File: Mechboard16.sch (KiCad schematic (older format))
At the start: 154 parts, among them CN1 CONN_C16, CN2 CONN_+4, SW0:0 KEY_DEL, SW0:1 KEY_RET, SW0:2 KEY_PND, SW0:3 KEY_HLP, SW0:4 KEY_F1, SW0:5 KEY_F2, SW0:6 KEY_F3, SW0:7 KEY_AT, SW1:0 KEY_3, SW1:1 KEY_W, SW1:2 KEY_A, SW1:3 KEY_4, SW1:4 KEY_Z, SW1:5 KEY_S, SW1:6 KEY_E, SW1:7 KEY_LSH, SW1B:7 KEY_RSH, SW1C:7 KEY_CLK, SW2:0 KEY_5, SW2:1 KEY_R, SW2:2 KEY_D, SW2:3 KEY_6, SW2:4 KEY_C, SW2:5 KEY_F, SW2:6 KEY_T, SW2:7 KEY_X, SW3:0 KEY_7, SW3:1 KEY_Y, SW3:2 KEY_G, SW3:3 KEY_8, SW3:4 KEY_B, SW3:5 KEY_H, SW3:6 KEY_U, SW3:7 KEY_V, SW4:0 KEY_9, SW4:1 KEY_I, SW4:2 KEY_J, SW4:3 KEY_0, SW4:4 KEY_M, SW4:5 KEY_K, SW4:6 KEY_O, SW4:7 KEY_N, SW5:0 KEY_DN, SW5:1 KEY_P, SW5:2 KEY_L, SW5:3 KEY_UP, SW5:4 KEY_DOT, SW5:5 KEY_COL, SW5:6 KEY_MIN, SW5:7 KEY_COM, SW6:0 KEY_LF, SW6:1 KEY_AST, SW6:2 KEY_SEM, SW6:3 KEY_RT, SW6:4 KEY_ESC, SW6:5 KEY_EQ, SW6:6 KEY_PLS, SW6:7 KEY_SLA, SW7:0 KEY_1, SW7:1 KEY_CLR, SW7:2 KEY_CTL, SW7:3 KEY_2, SW7:4 KEY_SPC, SW7:5 KEY_CMD, SW7:6 KEY_Q, SW7:7 KEY_RUN, SW7B:2 KEY_CTL_2, U1 4066, U2 NE555, U3 RP2040_Zero

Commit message: Add ATmega32U4, MAX7221 and leeeeeds! Routing TBD ^___^
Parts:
- removed SW7B:2: KEY_CTL_2, Mechboard16:SW_Cherry_MX_PCB_1.50u, symbol Switch:SW_Push_45deg
- removed U3: RP2040_Zero, Mechboard16:rp2040-zero, symbol RP2040_Zero:RP2040_Zero
- LD1: value LED -> LED_CLK
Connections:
- net labels added: col[0..7], row[0..7]
- wire segments 469 -> 462
- no-connect marks 14 -> 9
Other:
- note removed: "NOTE: If U3 is mounted, do NOT \nconnect keyboard to computer\nvia CN1/2!"
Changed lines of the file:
@@
 $Descr A4 11693 8268
 encoding utf-8
-Sheet 1 1
+Sheet 1 2
 Title "Mechboard16"
-Date "2023-10-13"
+Date "2023-11-25"
 Rev "1git"
 Comp "SukkoPera"
@@
 	5260 6850 5680 6850
 $Comp
-L power:GND #PWR0103
+L power:GND #PWR06
 U 1 1 66EB0AEA
 P 5260 7470
-F 0 "#PWR0103" H 5260 7220 50  0001 C CNN
+F 0 "#PWR06" H 5260 7220 50  0001 C CNN
 F 1 "GND" H 5265 7297 50  0000 C CNN
 F 2 "" H 5260 7470 50  0001 C CNN
@@
 	6465 2880 6770 2880
 $Comp
-L power:GND #PWR0104
+L power:GND #PWR05
 U 1 1 67015259
 P 6465 4160
-F 0 "#PWR0104" H 6465 3910 50  0001 C CNN
+F 0 "#PWR05" H 6465 3910 50  0001 C CNN
 F 1 "GND" H 6470 3987 50  0000 C CNN
 F 2 "" H 6465 4160 50  0001 C CNN
@@
 	1    0    0    -1
 $EndComp
-Wire Wire Line
-	7245 3600 7245 3650
 $Comp
 L power:GND #PWR0107
@@
 P 9670 5870
 F 0 "LD1" V 9709 5752 50  0000 R CNN
-F 1 "LED" V 9618 5752 50  0000 R CNN
+F 1 "LED_CLK" V 9618 5752 50  0000 R CNN
 F 2 "LED_THT:LED_D3.0mm" H 9670 5870 50  0001 C CNN
 F 3 "~" H 9670 5870 50  0001 C CNN
@@
 Wire Wire Line
 	7245 3235 7245 3175
-$Comp
-L power:PWR_FLAG #FLG0102
-U 1 1 680610F8
-P 7245 3650
-F 0 "#FLG0102" H 7245 3725 50  0001 C CNN
-F 1 "PWR_FLAG" V 7245 3778 50  0000 L CNN
-F 2 "" H 7245 3650 50  0001 C CNN
-F 3 "~" H 7245 3650 50  0001 C CNN
-	1    7245 3650
-	0    1    1    0
-$EndComp
-Connection ~ 7245 3650
-Wire Wire Line
-	7245 3650 7245 3695
 Text Notes 8205 1225 2    50   ~ 0
 Note that the C16 does not\nhave power on the keyboard\nconnector! A bodge wire mod\nwill be needed!\nFor LittleSixteen, we'll add a\njumper in the next release.
@@
 	0    1    1    0
 $EndComp
+Text Notes 3825 6255 0    50   ~ 0
+MOUNTING\nHOLES
+Text Label 2675 4835 0    50   ~ 0
+ctl_a
+Text Label 2875 5235 1    50   ~ 0
+ctl_b
+$Sheet
+S 1460 7125 955  490
+U 656CF65E
+F0 "USB Controller" 50
+F1 "usb.sch" 50
+$EndSheet
+Text GLabel 2655 5975 2    50   Output ~ 0
+col[0..7]
+Wire Bus Line
+	2190 5975 2655 5975
+Entry Wire Line
+	2190 6805 2290 6905
+Entry Wire Line
+	2190 6705 2290 6805
+Entry Wire Line
+	2190 6605 2290 6705
+Entry Wire Line
+	2190 6505 2290 6605
+Entry Wire Line
+	2190 6405 2290 6505
+Entry Wire Line
+	2190 6305 2290 6405
+Entry Wire Line
+	2190 6205 2290 6305
+Entry Wire Line
+	2190 6105 2290 6205
+Text GLabel 1250 5975 0    50   BiDi ~ 0
+row[0..7]
+Wire Bus Line
+	1715 5975 1250 5975
+Entry Wire Line
+	1715 6805 1615 6905
+Entry Wire Line
+	1715 6705 1615 6805
+Entry Wire Line
+	1715 6605 1615 6705
+Entry Wire Line
+	1715 6505 1615 6605
+Entry Wire Line
+	1715 6405 1615 6505
+Entry Wire Line
+	1715 6305 1615 6405
+Entry Wire Line
+	1715 6205 1615 6305
+Entry Wire Line
+	1715 6105 1615 6205
+Text Notes 1440 5610 0    50   ~ 0
+USB KEYBOARD CONTROLLER
+Text Label 2675 6205 2    50   ~ 0
+col7
+Text Label 2675 6305 2    50   ~ 0
+col6
+Text Label 2675 6405 2    50   ~ 0
+col5
+Text Label 2675 6505 2    50   ~ 0
+col4
+Text Label 2675 6605 2    50   ~ 0
+col3
+Text Label 2675 6705 2    50   ~ 0
+col2
+Text Label 2675 6805 2    50   ~ 0
+col1
+Text Label 2675 6905 2    50   ~ 0
+col0
+Text Label 1230 6905 0    50   ~ 0
+row7
+Text Label 1230 6805 0    50   ~ 0
+row6
+Text Label 1230 6705 0    50   ~ 0
+row5
+Text Label 1230 6605 0    50   ~ 0
+row4
+Text Label 1230 6505 0    50   ~ 0
+row3
+Text Label 1230 6405 0    50   ~ 0
+row2
+Text Label 1230 6305 0    50   ~ 0
+row1
+Text Label 1230 6205 0    50   ~ 0
+row0
 Wire Wire Line
-	950  6055 850  6055
-Wire Wire Line
-	850  6055 850  5755
-Wire Wire Line
-	950  6155 850  6155
-Wire Wire Line
-	850  6155 850  7405
-$Comp
-L power:GND #PWR06
-U 1 1 68E3A75D
-P 850 7405
-F 0 "#PWR06" H 850 7155 50  0001 C CNN
-F 1 "GND" H 855 7232 50  0000 C CNN
-F 2 "" H 850 7405 50  0001 C CNN
-F 3 "" H 850 7405 50  0001 C CNN
-	1    850  7405
-	1    0    0    -1
-$EndComp
-$Comp
-L power:+5V #PWR05
-U 1 1 68E3AF82
-P 850 5755
-F 0 "#PWR05" H 850 5605 50  0001 C CNN
-F 1 "+5V" H 865 5928 50  0000 C CNN
-F 2 "" H 850 5755 50  0001 C CNN
-F 3 "" H 850 5755 50  0001 C CNN
-	1    850  5755
-	1    0    0    -1
-$EndComp
-NoConn ~ 950  6255
-NoConn ~ 950  6355
-NoConn ~ 950  6455
-NoConn ~ 950  6555
-NoConn ~ 950  6655
-Wire Wire Line
-	2950 6055 3335 6055
-Wire Wire Line
-	2950 6155 3335 6155
+	2675 6805 2290 6805
 Wire Wire Line
-	2950 6255 3335 6255
+	2675 6705 2290 6705
 Wire Wire Line
-	2950 6355 3335 6355
+	2675 6605 2290 6605
 Wire Wire Line
-	2950 6455 3335 6455
+	2675 6505 2290 6505
 Wire Wire Line
-	2950 6555 3335 6555
+	2675 6405 2290 6405
 Wire Wire Line
-	2950 6655 3335 6655
+	2675 6305 2290 6305
 Wire Wire Line
-	2950 6755 3335 6755
+	2675 6205 2290 6205
 Wire Wire Line
-	2950 6855 3335 6855
+	2290 6905 2675 6905
 Wire Wire Line
-	565  6755 950  6755
+	1615 6905 1230 6905
 Wire Wire Line
-	565  6855 950  6855
+	1615 6805 1230 6805
 Wire Wire Line
-	1750 7740 1750 7355
+	1615 6705 1230 6705
 Wire Wire Line
-	1850 7740 1850 7355
+	1615 6605 1230 6605
 Wire Wire Line
-	1950 7740 1950 7355
+	1615 6505 1230 6505
 Wire Wire Line
-	2050 7740 2050 7355
+	1615 6405 1230 6405
 Wire Wire Line
-	2150 7740 2150 7355
-Text Label 3335 6055 2    50   ~ 0
-row0
-Text Label 3335 6155 2    50   ~ 0
-row1
-Text Label 3335 6255 2    50   ~ 0
-row2
-Text Label 3335 6355 2    50   ~ 0
-row3
-Text Label 3335 6455 2    50   ~ 0
-row4
-Text Label 3335 6555 2    50   ~ 0
-row5
-Text Label 3335 6655 2    50   ~ 0
-row6
-Text Label 3335 6755 2    50   ~ 0
-row7
-Text Label 3335 6855 2    50   ~ 0
-col0
-Text Label 2150 7740 1    50   ~ 0
-col1
-Text Label 2050 7740 1    50   ~ 0
-col2
-Text Label 1950 7740 1    50   ~ 0
-col3
-Text Label 1850 7740 1    50   ~ 0
-col4
-Text Label 1750 7740 1    50   ~ 0
-col5
-Text Label 565  6855 0    50   ~ 0
-col6
-Text Label 565  6755 0    50   ~ 0
-col7
-Text Notes 3825 6255 0    50   ~ 0
-MOUNTING\nHOLES
-Text Notes 1440 5610 0    50   ~ 0
-USB KEYBOARD CONTROLLER
-Text Notes 2275 7395 0    50   ~ 0
-NOTE: If U3 is mounted, do NOT \nconnect keyboard to computer\nvia CN1/2!
-$Comp
-L RP2040_Zero:RP2040_Zero U3
-U 1 1 68DDCE04
-P 1950 6455
-F 0 "U3" H 1950 7220 50  0000 C CNN
-F 1 "RP2040_Zero" H 1950 7129 50  0000 C CNN
-F 2 "Mechboard16:rp2040-zero" H 1950 6455 50  0001 C CNN
-F 3 "https://www.waveshare.com/wiki/RP2040-Zero" H 1950 6455 50  0001 C CNN
-	1    1950 6455
-	1    0    0    -1
-$EndComp
-$Comp
-L Switch:SW_Push_45deg SW7B:2
-U 1 1 6971412A
-P 6200 980
-F 0 "SW7B:2" H 6275 1135 50  0000 C CIN
-F 1 "KEY_CTL_2" V 6020 980 50  0000 C CNN
-F 2 "Mechboard16:SW_Cherry_MX_PCB_1.50u" H 6200 980 50  0001 C CNN
-F 3 "~" H 6200 980 50  0001 C CNN
-	1    6200 980
-	1    0    0    -1
-$EndComp
+	1615 6305 1230 6305
 Wire Wire Line
-	6100 880  6100 775
-Text Label 6100 775  0    50   ~ 0
-ctl_a
-Text Label 2675 4835 0    50   ~ 0
-ctl_a
-Text Label 2875 5235 1    50   ~ 0
-ctl_b
-Text Label 6515 1080 2    50   ~ 0
-ctl_b
+	1615 6205 1230 6205
 Wire Wire Line
-	6300 1080 6515 1080
+	7245 3600 7245 3695
+Wire Bus Line
+	2190 5975 2190 6805
+Wire Bus Line
+	1715 5975 1715 6805
 $EndSCHEMATC

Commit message: LED routing in progress...
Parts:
- SW0:3, SW0:4, SW0:5, SW0:6, SW1:7, SW1B:7, SW7:2: footprint Mechboard16:SW_Cherry_MX_PCB_1.50u -> Mechboard16:SW_Cherry_MX_PCB_1.50u_OffsetR
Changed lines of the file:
@@
 F 0 "SW7:2" H 2855 5190 50  0000 C CNN
 F 1 "KEY_CTL" V 2595 5035 50  0000 C CNN
-F 2 "Mechboard16:SW_Cherry_MX_PCB_1.50u" H 2775 5035 50  0001 C CNN
+F 2 "Mechboard16:SW_Cherry_MX_PCB_1.50u_OffsetR" H 2775 5035 50  0001 C CNN
 F 3 "~" H 2775 5035 50  0001 C CNN
 	1    2775 5035
@@
 F 0 "SW0:3" H 3350 1690 50  0000 C CNN
 F 1 "KEY_HLP" V 3095 1535 50  0000 C CNN
-F 2 "Mechboard16:SW_Cherry_MX_PCB_1.50u" H 3275 1535 50  0001 C CNN
+F 2 "Mechboard16:SW_Cherry_MX_PCB_1.50u_OffsetR" H 3275 1535 50  0001 C CNN
 F 3 "~" H 3275 1535 50  0001 C CNN
 	1    3275 1535
@@
 F 0 "SW0:4" H 3850 1690 50  0000 C CNN
 F 1 "KEY_F1" V 3595 1535 50  0000 C CNN
-F 2 "Mechboard16:SW_Cherry_MX_PCB_1.50u" H 3775 1535 50  0001 C CNN
+F 2 "Mechboard16:SW_Cherry_MX_PCB_1.50u_OffsetR" H 3775 1535 50  0001 C CNN
 F 3 "~" H 3775 1535 50  0001 C CNN
 	1    3775 1535
@@
 F 0 "SW0:5" H 4350 1690 50  0000 C CNN
 F 1 "KEY_F2" V 4095 1535 50  0000 C CNN
-F 2 "Mechboard16:SW_Cherry_MX_PCB_1.50u" H 4275 1535 50  0001 C CNN
+F 2 "Mechboard16:SW_Cherry_MX_PCB_1.50u_OffsetR" H 4275 1535 50  0001 C CNN
 F 3 "~" H 4275 1535 50  0001 C CNN
 	1    4275 1535
@@
 F 0 "SW0:6" H 4850 1690 50  0000 C CNN
 F 1 "KEY_F3" V 4595 1535 50  0000 C CNN
-F 2 "Mechboard16:SW_Cherry_MX_PCB_1.50u" H 4775 1535 50  0001 C CNN
+F 2 "Mechboard16:SW_Cherry_MX_PCB_1.50u_OffsetR" H 4775 1535 50  0001 C CNN
 F 3 "~" H 4775 1535 50  0001 C CNN
 	1    4775 1535
@@
 F 0 "SW1:7" H 5355 2190 50  0000 C CNN
 F 1 "KEY_LSH" V 5095 2035 50  0000 C CNN
-F 2 "Mechboard16:SW_Cherry_MX_PCB_1.50u" H 5275 2035 50  0001 C CNN
+F 2 "Mechboard16:SW_Cherry_MX_PCB_1.50u_OffsetR" H 5275 2035 50  0001 C CNN
 F 3 "~" H 5275 2035 50  0001 C CNN
 	1    5275 2035
@@
 F 0 "SW1B:7" H 5855 2190 50  0000 C CNN
 F 1 "KEY_RSH" V 5595 2035 50  0000 C CNN
-F 2 "Mechboard16:SW_Cherry_MX_PCB_1.50u" H 5775 2035 50  0001 C CNN
+F 2 "Mechboard16:SW_Cherry_MX_PCB_1.50u_OffsetR" H 5775 2035 50  0001 C CNN
 F 3 "~" H 5775 2035 50  0001 C CNN
 	1    5775 2035

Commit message: Routing in progress
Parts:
- SW7:4: footprint Mechboard16:SW_Cherry_MX_PCB_1.00u -> Mechboard16:SW_Cherry_MX_PCB_9.00u
- renumbered LD1 to LD1C:7
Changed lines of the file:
@@
 F 0 "SW7:4" H 3855 5190 50  0000 C CNN
 F 1 "KEY_SPC" V 3595 5035 50  0000 C CNN
-F 2 "Mechboard16:SW_Cherry_MX_PCB_1.00u" H 3775 5035 50  0001 C CNN
+F 2 "Mechboard16:SW_Cherry_MX_PCB_9.00u" H 3775 5035 50  0001 C CNN
 F 3 "~" H 3775 5035 50  0001 C CNN
 	1    3775 5035
@@
 	9670 5665 9670 5720
 $Comp
-L Device:LED LD1
+L Device:LED LD1C:7
 U 1 1 6726E132
 P 9670 5870
-F 0 "LD1" V 9709 5752 50  0000 R CNN
+F 0 "LD1C:7" V 9709 5752 50  0000 R CNN
 F 1 "LED_CLK" V 9618 5752 50  0000 R CNN
 F 2 "LED_THT:LED_D3.0mm" H 9670 5870 50  0001 C CNN

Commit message: IN PRODUCTION!
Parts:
- R3: value 56 -> 1k; LCSC C17557 -> C17513
- U1: LCSC C412482 -> C233577
- U2: LCSC C181735 -> C5125085
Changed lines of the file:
@@
 F 2 "Package_SO:SOIC-14_3.9x8.7mm_P1.27mm" H 10225 5235 50  0001 C CNN
 F 3 "http://www.ti.com/lit/ds/symlink/cd4066b.pdf" H 10225 5235 50  0001 C CNN
-F 4 "C412482" H 10225 5235 50  0001 C CNN "LCSC"
+F 4 "C233577" H 10225 5235 50  0001 C CNN "LCSC"
 	1    10225 5235
 	0    -1   -1   0
@@
 F 2 "Package_SO:SOIC-14_3.9x8.7mm_P1.27mm" H 5680 7260 50  0001 C CNN
 F 3 "http://www.ti.com/lit/ds/symlink/cd4066b.pdf" H 5680 7260 50  0001 C CNN
-F 4 "C412482" H 5680 7260 50  0001 C CNN "LCSC"
+F 4 "C233577" H 5680 7260 50  0001 C CNN "LCSC"
 	2    5680 7260
 	1    0    0    -1
@@
 F 2 "Package_SO:SOIC-14_3.9x8.7mm_P1.27mm" H 4855 7260 50  0001 C CNN
 F 3 "http://www.ti.com/lit/ds/symlink/cd4066b.pdf" H 4855 7260 50  0001 C CNN
-F 4 "C412482" H 4855 7260 50  0001 C CNN "LCSC"
+F 4 "C233577" H 4855 7260 50  0001 C CNN "LCSC"
 	3    4855 7260
 	1    0    0    -1
@@
 F 2 "Package_SO:SOIC-14_3.9x8.7mm_P1.27mm" H 6560 7260 50  0001 C CNN
 F 3 "http://www.ti.com/lit/ds/symlink/cd4066b.pdf" H 6560 7260 50  0001 C CNN
-F 4 "C412482" H 6560 7260 50  0001 C CNN "LCSC"
+F 4 "C233577" H 6560 7260 50  0001 C CNN "LCSC"
 	4    6560 7260
 	1    0    0    -1
@@
 F 2 "Package_SO:SOIC-14_3.9x8.7mm_P1.27mm" H 6155 3440 50  0001 C CNN
 F 3 "http://www.ti.com/lit/ds/symlink/cd4066b.pdf" H 6155 3440 50  0001 C CNN
-F 4 "C412482" H 6155 3440 50  0001 C CNN "LCSC"
+F 4 "C233577" H 6155 3440 50  0001 C CNN "LCSC"
 	5    6155 3440
 	1    0    0    -1
@@
 F 2 "Package_SO:SOIC-8_3.9x4.9mm_P1.27mm" H 9740 5035 50  0001 C CNN
 F 3 "http://www.ti.com/lit/ds/symlink/ne555.pdf" H 9740 5035 50  0001 C CNN
-F 4 "C181735" H 8890 5435 50  0001 C CNN "LCSC"
+F 4 "C5125085" H 8890 5435 50  0001 C CNN "LCSC"
 	1    8890 5435
 	1    0    0    -1
@@
 P 9670 5515
 F 0 "R3" H 9600 5469 50  0000 R CNN
-F 1 "56" H 9600 5560 50  0000 R CNN
+F 1 "1k" H 9600 5560 50  0000 R CNN
 F 2 "Resistor_SMD:R_0805_2012Metric_Pad1.20x1.40mm_HandSolder" V 9600 5515 50  0001 C CNN
 F 3 "~" H 9670 5515 50  0001 C CNN
-F 4 "C17557" H 9670 5515 50  0001 C CNN "LCSC"
+F 4 "C17513" H 9670 5515 50  0001 C CNN "LCSC"
 	1    9670 5515
 	-1   0    0    1

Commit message: R3 done
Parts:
- SW0:0, SW0:2, SW0:7, SW1:0, SW1:1, SW1:2, SW1:3, SW1:4, SW1:5, SW1:6, SW1C:7, SW2:0, SW2:1, SW2:2, SW2:3, SW2:4, SW2:5, SW2:6, SW2:7, SW3:0, SW3:1, SW3:2, SW3:3, SW3:4, SW3:5, SW3:6, SW3:7, SW4:0, SW4:1, SW4:2, SW4:3, SW4:4, SW4:5, SW4:6, SW4:7, SW5:0, SW5:1, SW5:2, SW5:3, SW5:4, SW5:5, SW5:6, SW5:7, SW6:0, SW6:1, SW6:2, SW6:3, SW6:4, SW6:5, SW6:6, SW6:7, SW7:0, SW7:1, SW7:3, SW7:5, SW7:6, SW7:7: footprint Mechboard16:SW_Cherry_MX_PCB_1.00u -> Mechboard16:SW_Hybrid_Cherry_MX_Alps_1.00u

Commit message: Switch non-1.00u keys to hybrid
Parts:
- SW0:1: footprint Mechboard16:SW_Cherry_MX_PCB_2.00u -> Mechboard16:SW_Hybrid_Cherry_MX_Alps_2.00u
- SW0:3, SW0:4, SW0:5, SW0:6, SW1:7, SW1B:7, SW7:2: footprint Mechboard16:SW_Cherry_MX_PCB_1.50u_OffsetR -> Mechboard16:SW_Hybrid_Cherry_MX_Alps_1.50u_OffsetR
- SW7:4: footprint Mechboard16:SW_Cherry_MX_PCB_9.00u -> Mechboard16:SW_Hybrid_Cherry_MX_Alps_9.00u
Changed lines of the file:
@@
 F 0 "SW0:1" H 2350 1690 50  0000 C CNN
 F 1 "KEY_RET" V 2095 1535 50  0000 C CNN
-F 2 "Mechboard16:SW_Cherry_MX_PCB_2.00u" H 2275 1535 50  0001 C CNN
+F 2 "Mechboard16:SW_Hybrid_Cherry_MX_Alps_2.00u" H 2275 1535 50  0001 C CNN
 F 3 "~" H 2275 1535 50  0001 C CNN
 	1    2275 1535
@@
 F 0 "SW7:2" H 2855 5190 50  0000 C CNN
 F 1 "KEY_CTL" V 2595 5035 50  0000 C CNN
-F 2 "Mechboard16:SW_Cherry_MX_PCB_1.50u_OffsetR" H 2775 5035 50  0001 C CNN
+F 2 "Mechboard16:SW_Hybrid_Cherry_MX_Alps_1.50u_OffsetR" H 2775 5035 50  0001 C CNN
 F 3 "~" H 2775 5035 50  0001 C CNN
 	1    2775 5035
@@
 F 0 "SW0:3" H 3350 1690 50  0000 C CNN
 F 1 "KEY_HLP" V 3095 1535 50  0000 C CNN
-F 2 "Mechboard16:SW_Cherry_MX_PCB_1.50u_OffsetR" H 3275 1535 50  0001 C CNN
+F 2 "Mechboard16:SW_Hybrid_Cherry_MX_Alps_1.50u_OffsetR" H 3275 1535 50  0001 C CNN
 F 3 "~" H 3275 1535 50  0001 C CNN
 	1    3275 1535
@@
 F 0 "SW0:4" H 3850 1690 50  0000 C CNN
 F 1 "KEY_F1" V 3595 1535 50  0000 C CNN
-F 2 "Mechboard16:SW_Cherry_MX_PCB_1.50u_OffsetR" H 3775 1535 50  0001 C CNN
+F 2 "Mechboard16:SW_Hybrid_Cherry_MX_Alps_1.50u_OffsetR" H 3775 1535 50  0001 C CNN
 F 3 "~" H 3775 1535 50  0001 C CNN
 	1    3775 1535
@@
 F 0 "SW7:4" H 3855 5190 50  0000 C CNN
 F 1 "KEY_SPC" V 3595 5035 50  0000 C CNN
-F 2 "Mechboard16:SW_Cherry_MX_PCB_9.00u" H 3775 5035 50  0001 C CNN
+F 2 "Mechboard16:SW_Hybrid_Cherry_MX_Alps_9.00u" H 3775 5035 50  0001 C CNN
 F 3 "~" H 3775 5035 50  0001 C CNN
 	1    3775 5035
@@
 F 0 "SW0:5" H 4350 1690 50  0000 C CNN
 F 1 "KEY_F2" V 4095 1535 50  0000 C CNN
-F 2 "Mechboard16:SW_Cherry_MX_PCB_1.50u_OffsetR" H 4275 1535 50  0001 C CNN
+F 2 "Mechboard16:SW_Hybrid_Cherry_MX_Alps_1.50u_OffsetR" H 4275 1535 50  0001 C CNN
 F 3 "~" H 4275 1535 50  0001 C CNN
 	1    4275 1535
@@
 F 0 "SW0:6" H 4850 1690 50  0000 C CNN
 F 1 "KEY_F3" V 4595 1535 50  0000 C CNN
-F 2 "Mechboard16:SW_Cherry_MX_PCB_1.50u_OffsetR" H 4775 1535 50  0001 C CNN
+F 2 "Mechboard16:SW_Hybrid_Cherry_MX_Alps_1.50u_OffsetR" H 4775 1535 50  0001 C CNN
 F 3 "~" H 4775 1535 50  0001 C CNN
 	1    4775 1535
@@
 F 0 "SW1:7" H 5355 2190 50  0000 C CNN
 F 1 "KEY_LSH" V 5095 2035 50  0000 C CNN
-F 2 "Mechboard16:SW_Cherry_MX_PCB_1.50u_OffsetR" H 5275 2035 50  0001 C CNN
+F 2 "Mechboard16:SW_Hybrid_Cherry_MX_Alps_1.50u_OffsetR" H 5275 2035 50  0001 C CNN
 F 3 "~" H 5275 2035 50  0001 C CNN
 	1    5275 2035
@@
 F 0 "SW1B:7" H 5855 2190 50  0000 C CNN
 F 1 "KEY_RSH" V 5595 2035 50  0000 C CNN
-F 2 "Mechboard16:SW_Cherry_MX_PCB_1.50u_OffsetR" H 5775 2035 50  0001 C CNN
+F 2 "Mechboard16:SW_Hybrid_Cherry_MX_Alps_1.50u_OffsetR" H 5775 2035 50  0001 C CNN
 F 3 "~" H 5775 2035 50  0001 C CNN
 	1    5775 2035

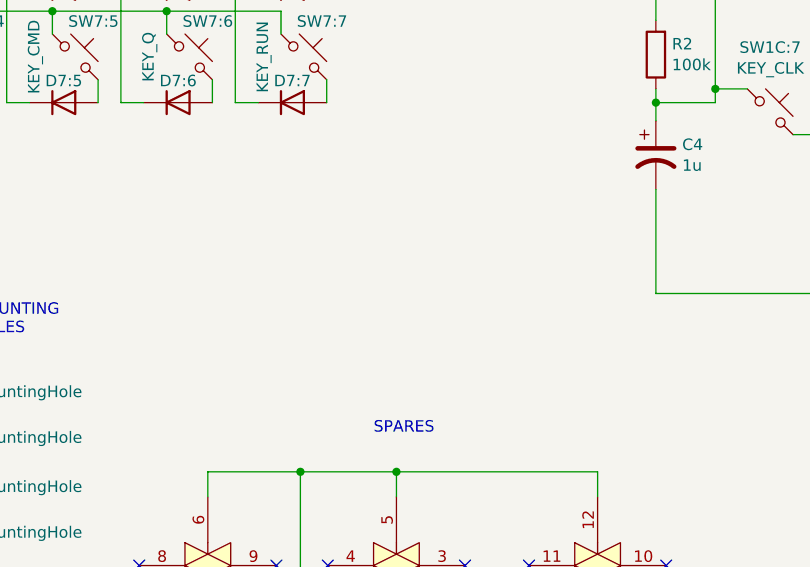
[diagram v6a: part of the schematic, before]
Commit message: Better stabilizer holes
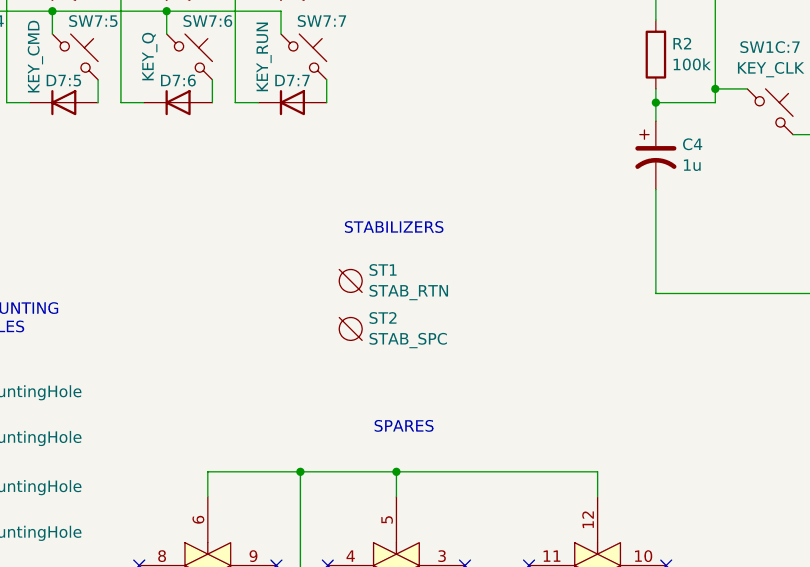
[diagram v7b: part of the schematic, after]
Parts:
- added ST1: STAB_RTN, Mechboard16:Stabilizer_Costar_2.00u, symbol void:Void
- added ST2: STAB_SPC, Mechboard16:Stabilizer_Costar_9.00u_Commodore, symbol void:Void
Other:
- note added: "STABILIZERS"
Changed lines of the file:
@@
 Sheet 1 2
 Title "Mechboard16"
-Date "2023-11-25"
+Date "2023-12-16"
 Rev "1git"
 Comp "SukkoPera"
@@
 Wire Wire Line
 	7245 3600 7245 3695
+$Comp
+L void:Void ST1
+U 1 1 65942D2A
+P 5480 6015
+F 0 "ST1" H 5558 6061 50  0000 L CNN
+F 1 "STAB_RTN" H 5558 5970 50  0000 L CNN
+F 2 "Mechboard16:Stabilizer_Costar_2.00u" H 5480 6015 50  0001 C CNN
+F 3 "" H 5480 6015 50  0001 C CNN
+	1    5480 6015
+	1    0    0    -1
+$EndComp
+$Comp
+L void:Void ST2
+U 1 1 65944191
+P 5480 6225
+F 0 "ST2" H 5558 6271 50  0000 L CNN
+F 1 "STAB_SPC" H 5558 6180 50  0000 L CNN
+F 2 "Mechboard16:Stabilizer_Costar_9.00u_Commodore" H 5480 6225 50  0001 C CNN
+F 3 "" H 5480 6225 50  0001 C CNN
+	1    5480 6225
+	1    0    0    -1
+$EndComp
 Wire Bus Line
 	2190 5975 2190 6805
 Wire Bus Line
 	1715 5975 1715 6805
+Text Notes 5450 5820 0    50   ~ 0
+STABILIZERS
 $EndSCHEMATC

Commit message: Back to MX-only and minor routing adjustments
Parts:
- SW0:0, SW0:2, SW0:7, SW1:0, SW1:1, SW1:2, SW1:3, SW1:4, SW1:5, SW1:6, SW1C:7, SW2:0, SW2:1, SW2:2, SW2:3, SW2:4, SW2:5, SW2:6, SW2:7, SW3:0, SW3:1, SW3:2, SW3:3, SW3:4, SW3:5, SW3:6, SW3:7, SW4:0, SW4:1, SW4:2, SW4:3, SW4:4, SW4:5, SW4:6, SW4:7, SW5:0, SW5:1, SW5:2, SW5:3, SW5:4, SW5:5, SW5:6, SW5:7, SW6:0, SW6:1, SW6:2, SW6:3, SW6:4, SW6:5, SW6:6, SW6:7, SW7:0, SW7:1, SW7:3, SW7:5, SW7:6, SW7:7: footprint Mechboard16:SW_Hybrid_Cherry_MX_Alps_1.00u -> Mechboard16:SW_Cherry_MX_PCB_1.00u
- SW0:1: footprint Mechboard16:SW_Hybrid_Cherry_MX_Alps_2.00u -> Mechboard16:SW_Cherry_MX_PCB_2.00u
- SW0:3, SW0:4, SW0:5, SW0:6, SW1:7, SW1B:7, SW7:2: footprint Mechboard16:SW_Hybrid_Cherry_MX_Alps_1.50u_OffsetR -> Mechboard16:SW_Cherry_MX_PCB_1.50u_OffsetR
- SW7:4: footprint Mechboard16:SW_Hybrid_Cherry_MX_Alps_9.00u -> Mechboard16:SW_Cherry_MX_PCB_9.00u
